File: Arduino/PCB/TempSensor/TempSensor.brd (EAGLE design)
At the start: 32.7 x 32.7 mm, 41 parts, among them IC1 DS1820, J1 FTDI_DEVICE, J2 FTDI_DEVICE, U1 ATMEGA328-AU, U2 LM2736X, U3 XC6210, X1 16Mhz

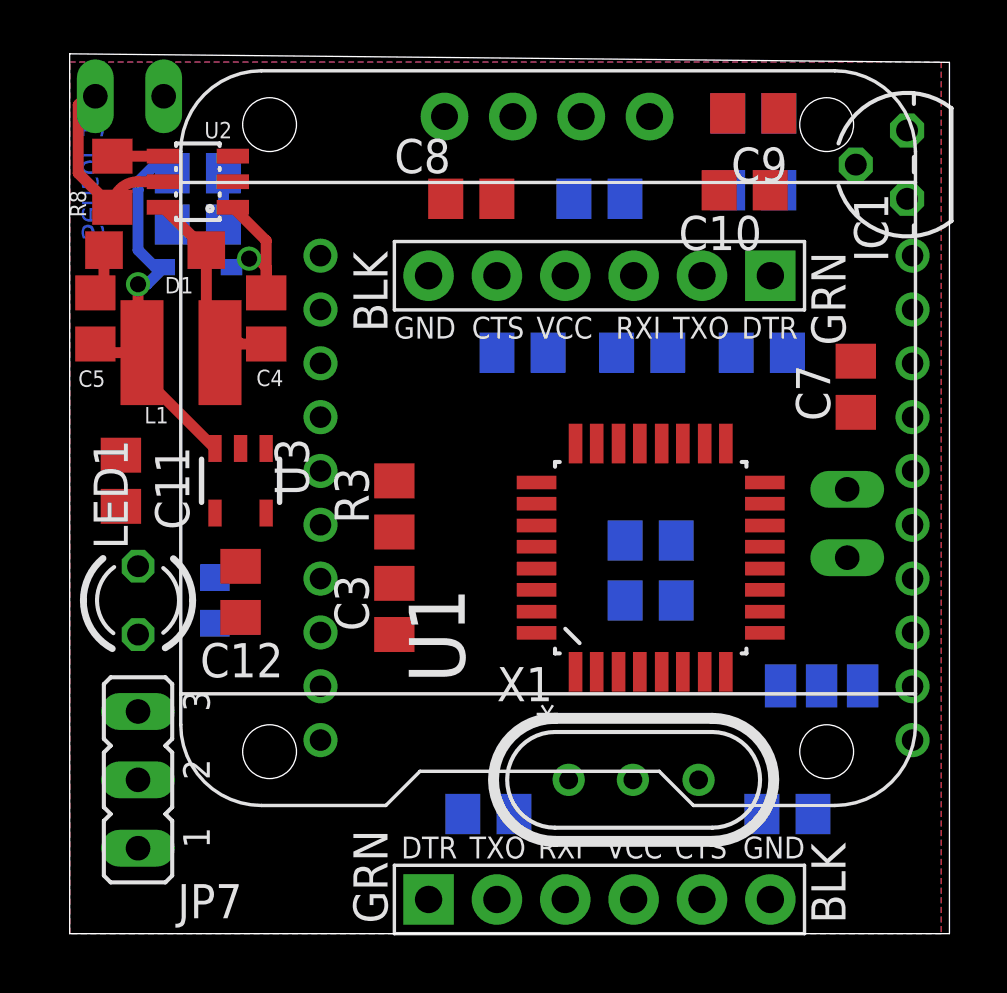
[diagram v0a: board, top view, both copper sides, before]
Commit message: 
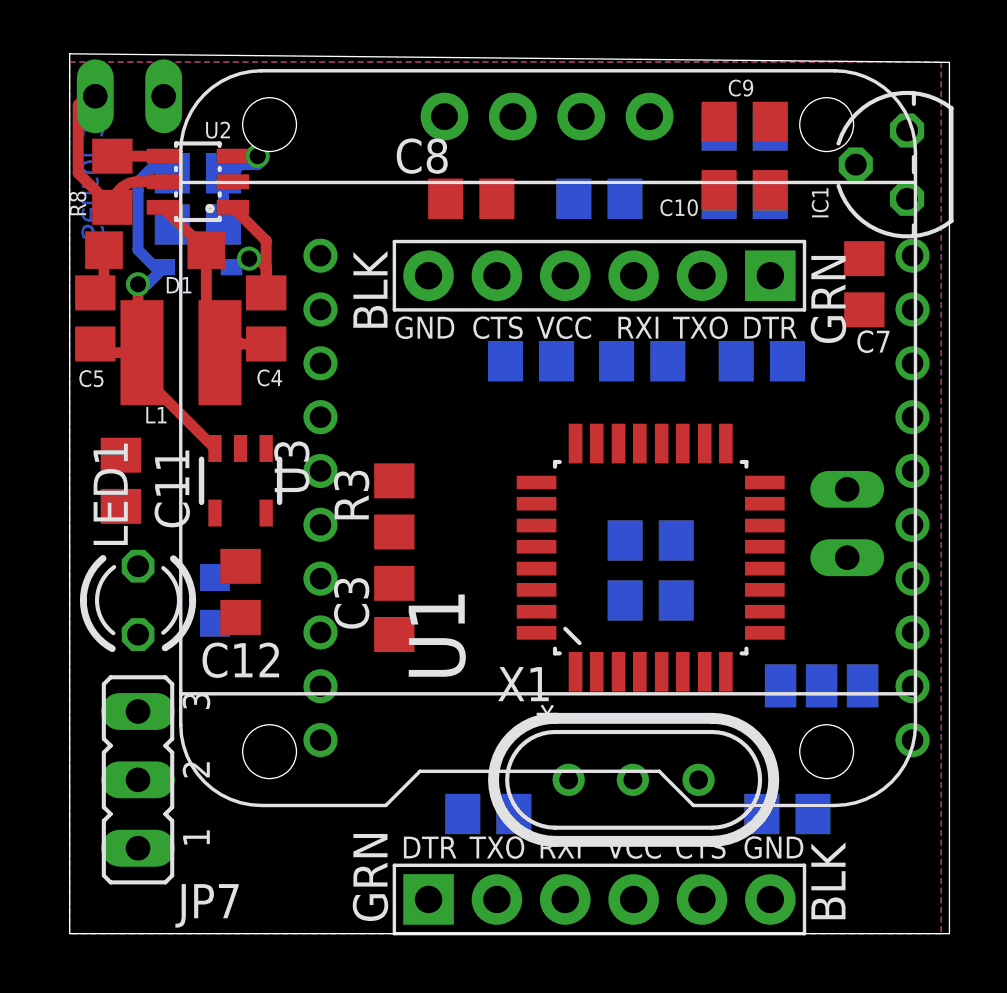
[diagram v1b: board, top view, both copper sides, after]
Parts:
- moved C7 3.82 mm to (66.4, 44.5), turned to 270 degrees
- moved R11 0.71 mm to (61.9, 50.2), turned to 0 degrees
- moved C6 0.45 mm to (54.0, 41.6)
- moved R13 0.45 mm to (61.9, 47.6), turned to 0 degrees
- moved C9 0.45 mm to (61.9, 50.5), turned to 0 degrees
- moved R1 0.32 mm to (62.5, 41.6)
- moved R4 0.32 mm to (58.1, 41.6)
- turned C10 to 0 degrees
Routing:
- net N$14: track 1.91 -> 4.61 mm, vias 0 -> 1

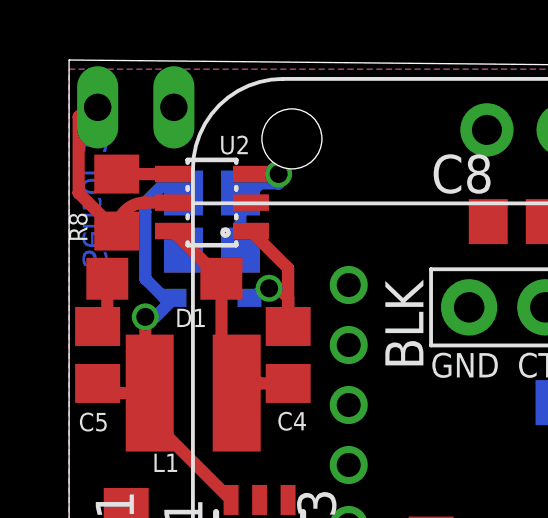
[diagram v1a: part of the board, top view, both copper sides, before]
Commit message: input cap toegevoegd
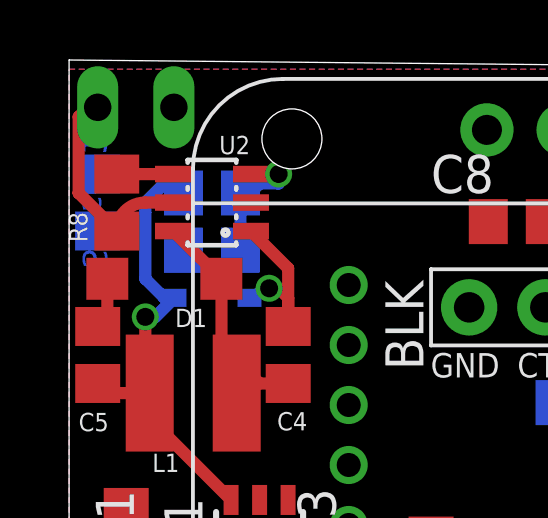
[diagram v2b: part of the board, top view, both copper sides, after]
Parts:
- added C13: 10u, rcl:C0805
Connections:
- net GND: now also C13.1
- net VIN: now also C13.2
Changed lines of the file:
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@@
 </element>
 <element name="JP6" library="jumper" package="JP1" value="" x="39.0525" y="51.435" smashed="yes" rot="MR270">
-<attribute name="NAME" x="35.8775" y="50.546" size="1.27" layer="26" ratio="10" rot="MR0"/>
+<attribute name="NAME" x="43.18" y="51.181" size="0.8128" layer="26" ratio="10" rot="MR0"/>
 <attribute name="VALUE" x="41.5925" y="48.514" size="1.27" layer="28" ratio="10" rot="MR0"/>
 </element>
@@
 <attribute name="NAME" x="44.7675" y="31.115" size="1.27" layer="25" rot="R180"/>
 <attribute name="VALUE" x="45.72" y="31.75" size="1.27" layer="27" rot="R90"/>
+</element>
+<element name="C13" library="rcl" package="C0805" value="10u" x="37.7825" y="48.26" smashed="yes" rot="MR90">
+<attribute name="NAME" x="38.4175" y="47.625" size="0.8128" layer="26" rot="MR90"/>
+<attribute name="VALUE" x="35.2425" y="46.99" size="1.27" layer="28" rot="MR90"/>
 </element>
 </elements>
@@
 <wire x1="38.105" y1="45.72" x2="38.105" y2="44.4525" width="0.4064" layer="1"/>
 <wire x1="38.105" y1="44.4525" x2="37.7825" y2="44.13" width="0.4064" layer="1"/>
-<wire x1="60.9625" y1="47.9425" x2="67.945" y2="47.625" width="0" layer="19" extent="1-1"/>
+<contactref element="C13" pad="1"/>
+<wire x1="66.3575" y1="45.4" x2="67.945" y2="47.625" width="0" layer="19" extent="1-1"/>
+<wire x1="60.9625" y1="47.9425" x2="66.3575" y2="45.4" width="0" layer="19" extent="1-1"/>
 <wire x1="60.9625" y1="50.4825" x2="60.9625" y2="47.9425" width="0" layer="19" extent="1-1"/>
-<wire x1="66.3575" y1="45.4" x2="67.945" y2="47.625" width="0" layer="19" extent="1-1"/>
-<wire x1="59.6138" y1="38.5318" x2="66.3575" y2="45.4" width="0" layer="19" extent="1-1"/>
+<wire x1="59.6138" y1="38.5318" x2="60.9625" y2="47.9425" width="0" layer="19" extent="1-1"/>
 <wire x1="58.0136" y1="38.5318" x2="59.6138" y2="38.5318" width="0" layer="19" extent="1-1"/>
 <wire x1="57.2262" y1="38.5318" x2="58.0136" y2="38.5318" width="0" layer="19" extent="1-1"/>
@@
 <wire x1="62.865" y1="21.59" x2="64.45" y2="24.765" width="0" layer="19" extent="16-16"/>
 <wire x1="51.4375" y1="24.765" x2="57.2262" y2="30.0482" width="0" layer="19" extent="1-16"/>
+<wire x1="37.7825" y1="47.31" x2="51.4375" y2="24.765" width="0" layer="19" extent="1-16"/>
 </signal>
 <signal name="N$1">
@@
 <wire x1="40.005" y1="48.26" x2="39.3675" y2="48.26" width="0.4064" layer="1"/>
 <wire x1="39.3675" y1="48.26" x2="38.4175" y2="47.31" width="0.4064" layer="1" curve="90"/>
+<contactref element="C13" pad="2"/>
+<wire x1="37.7825" y1="49.21" x2="42.2275" y2="50.4825" width="0" layer="19" extent="1-16"/>
+<wire x1="42.2275" y1="50.4825" x2="40.2925" y2="48.26" width="0" layer="19" extent="1-16"/>
 </signal>
 <signal name="N$19" class="1">

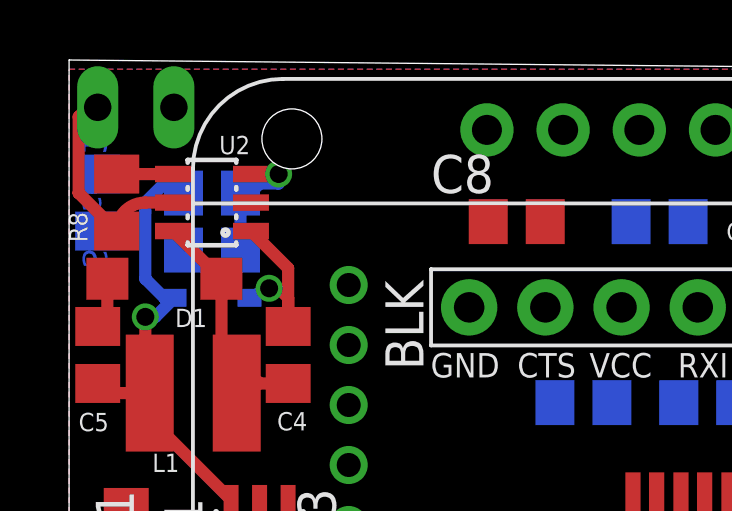
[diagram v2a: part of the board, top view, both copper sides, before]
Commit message: 
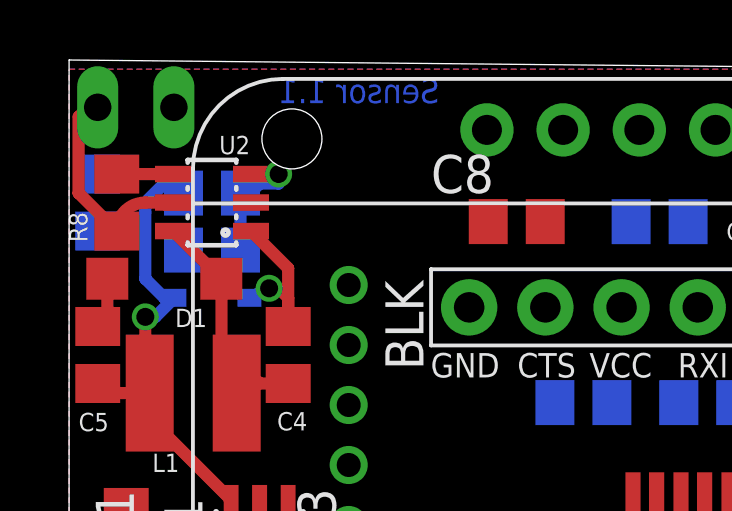
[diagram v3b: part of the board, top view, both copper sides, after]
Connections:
- net N$8 renamed SDA
- net N$9 renamed SCL
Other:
- board text added: "Sensor 1.1"
- board text removed: "Sensor 1.0"
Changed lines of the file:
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@@
 <grid distance="0.0125" unitdist="inch" unit="mm" style="lines" multiple="1" display="yes" altdistance="0.025" altunitdist="inch" altunit="inch"/>
 <layers>
-<layer number="1" name="Top" color="4" fill="1" visible="yes" active="yes"/>
+<layer number="1" name="Top" color="4" fill="1" visible="no" active="yes"/>
 <layer number="16" name="Bottom" color="1" fill="1" visible="yes" active="yes"/>
 <layer number="17" name="Pads" color="2" fill="1" visible="yes" active="yes"/>
@@
 <layer number="23" name="tOrigins" color="15" fill="1" visible="yes" active="yes"/>
 <layer number="24" name="bOrigins" color="15" fill="1" visible="yes" active="yes"/>
-<layer number="25" name="tNames" color="7" fill="1" visible="yes" active="yes"/>
-<layer number="26" name="bNames" color="7" fill="1" visible="yes" active="yes"/>
+<layer number="25" name="tNames" color="7" fill="1" visible="no" active="yes"/>
+<layer number="26" name="bNames" color="7" fill="1" visible="no" active="yes"/>
 <layer number="27" name="tValues" color="7" fill="1" visible="no" active="yes"/>
 <layer number="28" name="bValues" color="7" fill="1" visible="no" active="yes"/>
@@
 <text x="41.021" y="43.18" size="1.27" layer="125" ratio="10" rot="R270">X1</text>
 <text x="60.96" y="27.94" size="1.27" layer="126" rot="MR90">XB1</text>
-<text x="38.1" y="51.435" size="0.8128" layer="16" rot="MR270">Sensor 1.0</text>
+<text x="43.815" y="52.3875" size="0.8128" layer="16" rot="MR180">Sensor 1.1</text>
 </plain>
 <attributes>
@@
 <wire x1="63.246" y1="29.5275" x2="59.6138" y2="30.0482" width="0" layer="19" extent="1-16"/>
 </signal>
-<signal name="N$8">
+<signal name="SDA">
 <contactref element="U$2" pad="SDA"/>
 <contactref element="U1" pad="27"/>
@@
 <wire x1="54.1782" y1="35.4838" x2="59.0525" y2="41.5925" width="0" layer="19" extent="1-16"/>
 </signal>
-<signal name="N$9">
+<signal name="SCL">
 <contactref element="U$2" pad="SCL"/>
 <contactref element="U1" pad="28"/>

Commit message: as Send to allpcb
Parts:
- moved C11 1.59 mm to (40.3, 37.1)
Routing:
- net GND: track 1.72 -> 179.4 mm, vias 0 -> 3
- net +3V3: track 0.00 -> 106.3 mm, vias 0 -> 2
- net N$18: track 0.00 -> 38.5 mm
- net N$5: track 0.00 -> 35.4 mm, vias 0 -> 1
- net N$6: track 0.00 -> 35.1 mm, vias 0 -> 1
- net SDA: track 0.00 -> 26.9 mm
- net N$22: track 0.00 -> 25.5 mm
- net N$16: track 0.00 -> 25.0 mm, vias 0 -> 1
- net N$12: track 0.00 -> 23.8 mm, vias 0 -> 1
- net N$20: track 0.00 -> 23.7 mm, vias 0 -> 1
- net SCL: track 0.00 -> 21.8 mm
- net N$4: track 0.00 -> 18.6 mm
- net N$3: track 0.00 -> 16.7 mm
- net N$26: track 0.00 -> 14.6 mm
- net N$24: track 0.00 -> 14.1 mm
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
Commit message: component values
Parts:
- C5: value 100n -> 10u
- R11, R13: value 560 -> 580
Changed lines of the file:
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@@
 <attribute name="VALUE" x="46.6725" y="41.91" size="1.27" layer="27" rot="R90"/>
 </element>
-<element name="C5" library="rcl" package="C0805" value="100n" x="37.7825" y="43.18" smashed="yes" rot="R270">
+<element name="C5" library="rcl" package="C0805" value="10u" x="37.7825" y="43.18" smashed="yes" rot="R270">
 <attribute name="NAME" x="37.1475" y="40.64" size="0.6096" layer="25"/>
 <attribute name="VALUE" x="35.2425" y="44.45" size="1.27" layer="27" rot="R270"/>
@@
 <attribute name="VALUE" x="60.6425" y="47.9425" size="1.27" layer="27"/>
 </element>
-<element name="R11" library="rcl" package="R0805" value="560" x="61.9125" y="50.165" smashed="yes" rot="MR0">
+<element name="R11" library="rcl" package="R0805" value="580" x="61.9125" y="50.165" smashed="yes" rot="MR0">
 <attribute name="NAME" x="61.2775" y="51.7525" size="0.6096" layer="26" rot="MR180"/>
 <attribute name="VALUE" x="62.5475" y="47.625" size="1.27" layer="28" rot="MR0"/>
@@
 <attribute name="VALUE" x="60.6425" y="45.4025" size="1.27" layer="27"/>
 </element>
-<element name="R13" library="rcl" package="R0805" value="560" x="61.9125" y="47.625" smashed="yes" rot="MR0">
+<element name="R13" library="rcl" package="R0805" value="580" x="61.9125" y="47.625" smashed="yes" rot="MR0">
 <attribute name="NAME" x="62.5475" y="48.5775" size="0.6096" layer="26" rot="MR0"/>
 <attribute name="VALUE" x="62.5475" y="45.085" size="1.27" layer="28" rot="MR0"/>

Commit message: part values
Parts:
- C10, C9: value 100n -> 220p
- R10: value 21K5 -> 10K
- R11, R13: value 580 -> 100
- R9: value 10K -> 21K5
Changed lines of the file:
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@@
 <layers>
 <layer number="1" name="Top" color="4" fill="1" visible="yes" active="yes"/>
-<layer number="16" name="Bottom" color="1" fill="1" visible="yes" active="yes"/>
+<layer number="16" name="Bottom" color="1" fill="1" visible="no" active="yes"/>
 <layer number="17" name="Pads" color="2" fill="1" visible="yes" active="yes"/>
 <layer number="18" name="Vias" color="2" fill="1" visible="yes" active="yes"/>
@@
 </element>
 <element name="C3" library="rcl" package="C0805" value="100n" x="48.895" y="32.385" smashed="yes" rot="R270">
-<attribute name="NAME" x="47.3075" y="33.655" size="0.6096" layer="25" rot="R270"/>
+<attribute name="NAME" x="47.3075" y="33.9725" size="0.6096" layer="25" rot="R270"/>
 <attribute name="VALUE" x="46.355" y="33.655" size="1.27" layer="27" rot="R270"/>
 </element>
@@
 <attribute name="VALUE" x="50.4825" y="45.085" size="1.27" layer="27"/>
 </element>
-<element name="R9" library="rcl" package="R0805" value="10K" x="41.5925" y="48.5775" smashed="yes" rot="MR0">
+<element name="R9" library="rcl" package="R0805" value="21K5" x="41.5925" y="48.5775" smashed="yes" rot="MR0">
 <attribute name="NAME" x="44.7675" y="48.26" size="0.6096" layer="26" rot="MR0"/>
 <attribute name="VALUE" x="42.2275" y="46.0375" size="1.27" layer="28" rot="MR0"/>
 </element>
-<element name="R10" library="rcl" package="R0805" value="21K5" x="41.5925" y="46.6725" smashed="yes" rot="MR180">
+<element name="R10" library="rcl" package="R0805" value="10K" x="41.5925" y="46.6725" smashed="yes" rot="MR180">
 <attribute name="NAME" x="43.815" y="47.3075" size="0.6096" layer="26" rot="MR180"/>
 <attribute name="VALUE" x="40.9575" y="49.2125" size="1.27" layer="28" rot="MR180"/>
@@
 </element>
 <element name="D1" library="Components" package="SOD123" value="RB161M-20TR" x="40.005" y="45.72" smashed="yes" rot="R180">
-<attribute name="NAME" x="43.645" y="45.99" size="0.6096" layer="25" rot="R180"/>
+<attribute name="NAME" x="37.6125" y="45.99" size="0.6096" layer="25" rot="R180"/>
 <attribute name="VALUE" x="41.105" y="48.02" size="1.27" layer="27" rot="R180"/>
 </element>
 <element name="D2" library="Components" package="SOD323_ST" value="BAT54HT1G" x="41.5925" y="45.085" smashed="yes" rot="MR0">
-<attribute name="NAME" x="41.9725" y="43.6125" size="0.6096" layer="26" rot="MR0"/>
+<attribute name="NAME" x="41.9725" y="43.93" size="0.6096" layer="26" rot="MR0"/>
 <attribute name="VALUE" x="43.2425" y="43.085" size="1.27" layer="28" rot="MR0"/>
 </element>
-<element name="C9" library="rcl" package="C0805" value="100n" x="61.9125" y="50.4825" smashed="yes">
+<element name="C9" library="rcl" package="C0805" value="220p" x="61.9125" y="50.4825" smashed="yes">
 <attribute name="NAME" x="61.595" y="51.1175" size="0.6096" layer="25"/>
 <attribute name="VALUE" x="60.6425" y="47.9425" size="1.27" layer="27"/>
 </element>
-<element name="R11" library="rcl" package="R0805" value="580" x="61.9125" y="50.165" smashed="yes" rot="MR0">
+<element name="R11" library="rcl" package="R0805" value="100" x="61.9125" y="50.165" smashed="yes" rot="MR0">
 <attribute name="NAME" x="61.2775" y="51.7525" size="0.6096" layer="26" rot="MR180"/>
 <attribute name="VALUE" x="62.5475" y="47.625" size="1.27" layer="28" rot="MR0"/>
 </element>
-<element name="C10" library="rcl" package="C0805" value="100n" x="61.9125" y="47.9425" smashed="yes">
+<element name="C10" library="rcl" package="C0805" value="220p" x="61.9125" y="47.9425" smashed="yes">
 <attribute name="NAME" x="58.7375" y="46.99" size="0.6096" layer="25"/>
 <attribute name="VALUE" x="60.6425" y="45.4025" size="1.27" layer="27"/>
 </element>
-<element name="R13" library="rcl" package="R0805" value="580" x="61.9125" y="47.625" smashed="yes" rot="MR0">
+<element name="R13" library="rcl" package="R0805" value="100" x="61.9125" y="47.625" smashed="yes" rot="MR0">
 <attribute name="NAME" x="62.5475" y="48.5775" size="0.6096" layer="26" rot="MR0"/>
 <attribute name="VALUE" x="62.5475" y="45.085" size="1.27" layer="28" rot="MR0"/>
